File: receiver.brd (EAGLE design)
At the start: 130.8 x 100 mm, 33 parts

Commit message: Last corrects.
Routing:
- net GND: track 340.4 -> 341.4 mm
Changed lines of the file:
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@@
 <drawing>
 <settings>
-<setting alwaysvectorfont="no"/>
+<setting alwaysvectorfont="yes"/>
 <setting verticaltext="up"/>
 </settings>
@@
 <wire x1="45.72" y1="25.4" x2="45.72" y2="30.48" width="0.254" layer="1"/>
 <wire x1="45.72" y1="30.48" x2="49.24" y2="34" width="0.254" layer="1"/>
-<wire x1="16.51" y1="6.35" x2="26.67" y2="6.35" width="0.254" layer="1"/>
 <wire x1="26.67" y1="6.35" x2="45.72" y2="25.4" width="0.254" layer="1"/>
 <wire x1="26.67" y1="73.66" x2="27.94" y2="74.93" width="0.254" layer="16"/>
@@
 <wire x1="28.575" y1="80.645" x2="61.1378" y2="80.645" width="0.254" layer="16"/>
 <wire x1="61.1378" y1="80.645" x2="67.818" y2="87.3252" width="0.254" layer="16"/>
+<wire x1="16.51" y1="6.35" x2="17.78" y2="5.08" width="0.254" layer="1"/>
+<wire x1="17.78" y1="5.08" x2="25.4" y2="5.08" width="0.254" layer="1"/>
+<wire x1="25.4" y1="5.08" x2="26.67" y2="6.35" width="0.254" layer="1"/>
 </signal>
 <signal name="N$2">

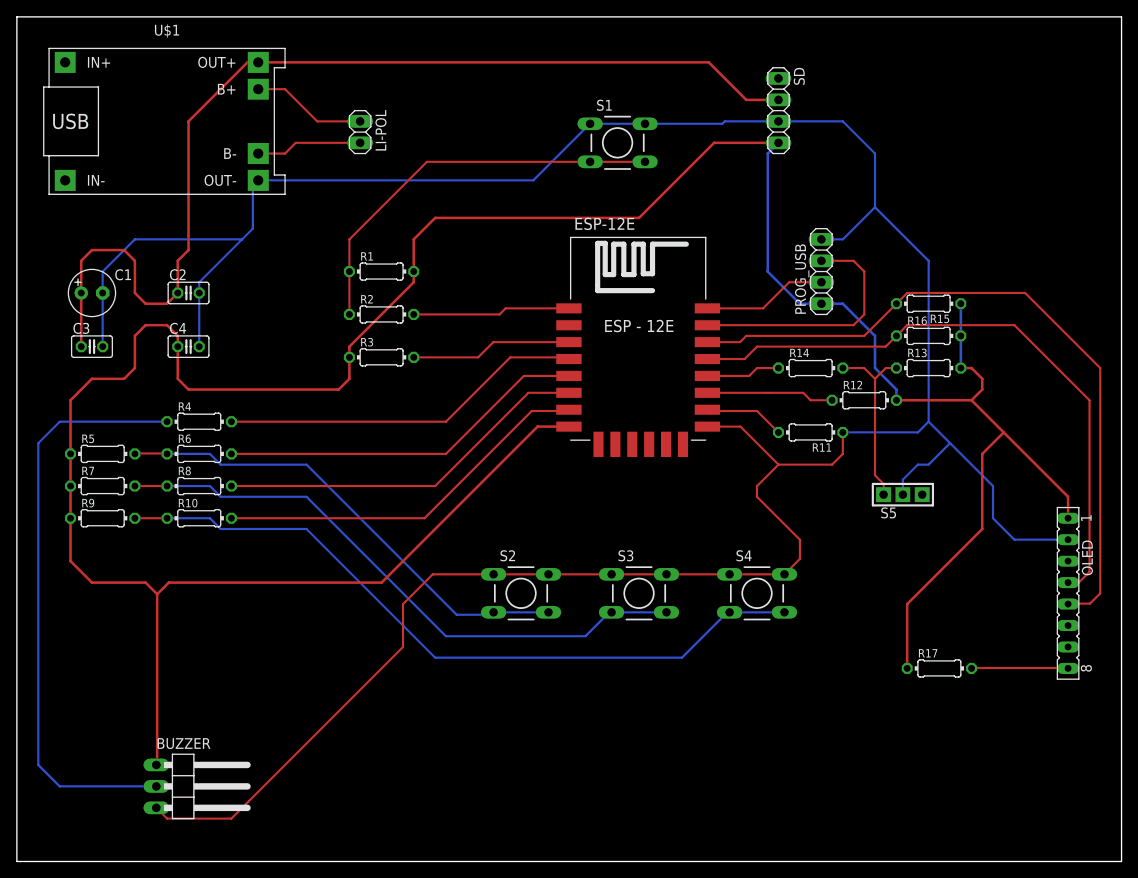
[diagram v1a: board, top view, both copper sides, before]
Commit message: Corrected programming switch connection.
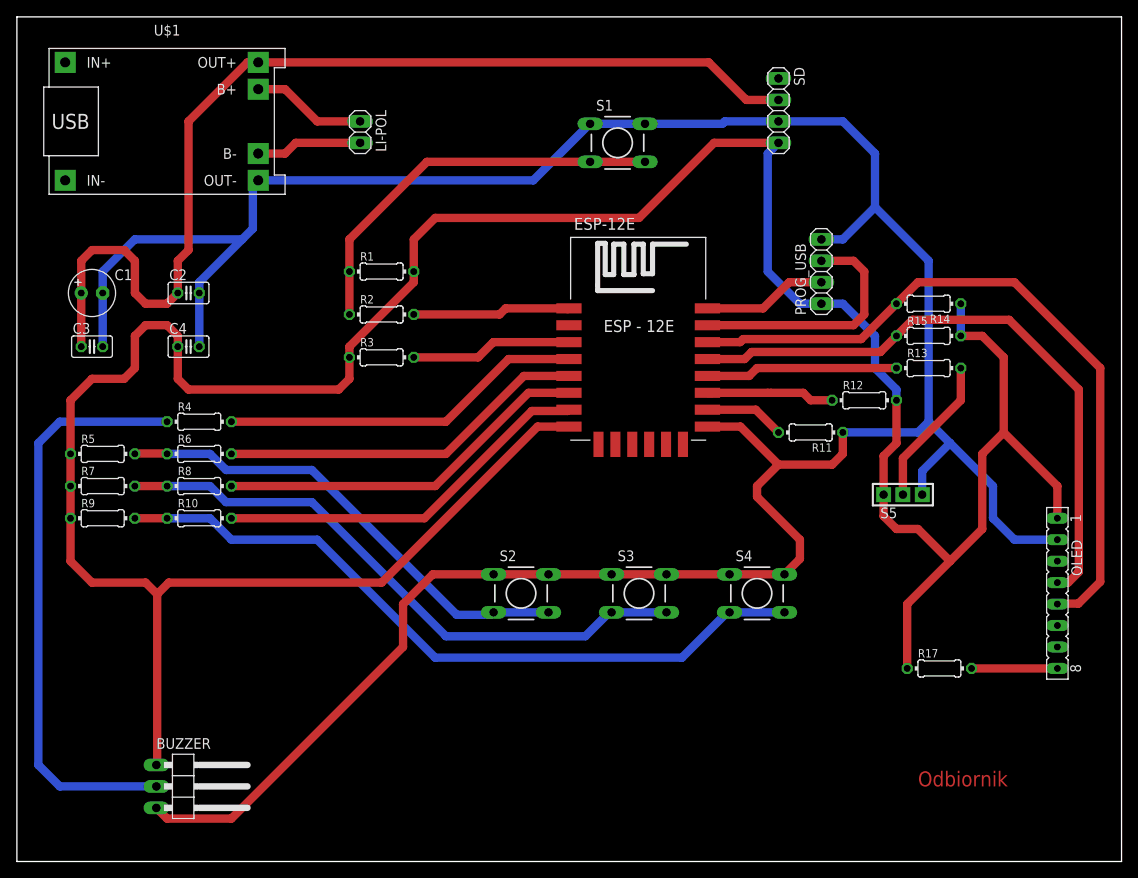
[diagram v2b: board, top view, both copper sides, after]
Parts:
- removed R16: 4,7k, rcl:0204/7
- R14: value 100 -> 4,7k
- moved R14 15.9 mm to (108.0, 66.0), turned to 180 degrees
- moved R15 3.81 mm to (108.0, 62.2), turned to 0 degrees
- moved OLED 1.27 mm to (123.2, 31.8)
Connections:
- net GND: now also S5.P$3; no longer S5.P$2
- net N$19: now also R13.1; no longer R14.1
- net N$3: now also R13.2, S5.P$2; no longer R13.1, R14.2, S5.P$1
- net SCL: now also R14.2; no longer R15.2
- net SDA: now also R15.1; no longer R16.1
- net VCC: now also R14.1, R15.2, S5.P$1; no longer R13.2, R15.1, R16.2
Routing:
- net VCC: track 337.1 -> 351.8 mm
- net N$19: track 8.80 -> 22.8 mm
- net N$3: track 21.7 -> 17.8 mm
- net N$8: track 13.9 -> 10.2 mm
- net GND: track 341.4 -> 338.5 mm
- net SCL: track 83.6 -> 85.1 mm
- net N$11: track 10.1 -> 9.52 mm
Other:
- board text added: "Odbiornik"
